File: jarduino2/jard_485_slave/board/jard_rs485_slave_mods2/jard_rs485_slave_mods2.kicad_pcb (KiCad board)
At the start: 2 copper layers, 79.2 x 30 mm, 43 parts, among them J1 POWER, J3 Débit, J4 Niveaux, J6 EV1, Q4 BPC_FMMT38C, Q6 P03P4L-04, U1 BPC_Mod485, U6 BPC_DHT22

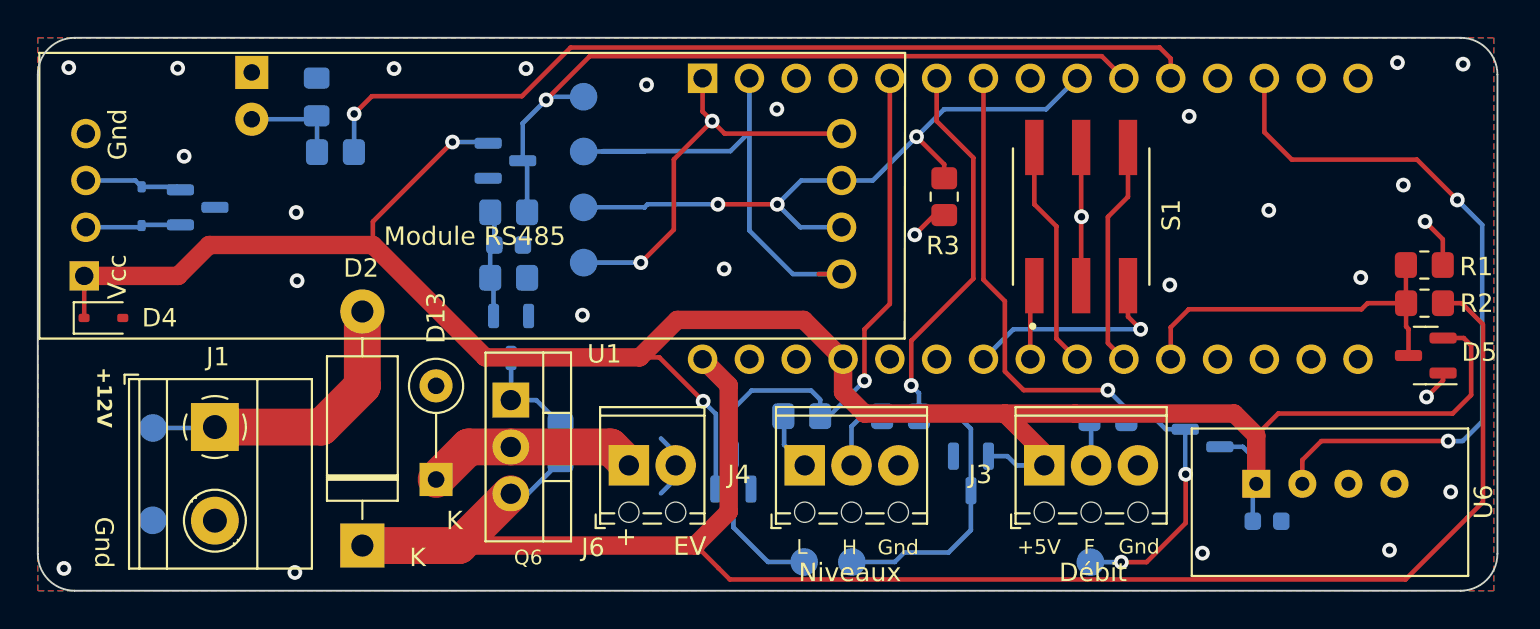
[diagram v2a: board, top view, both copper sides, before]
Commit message: Agrandissement pastilles Mod RS485
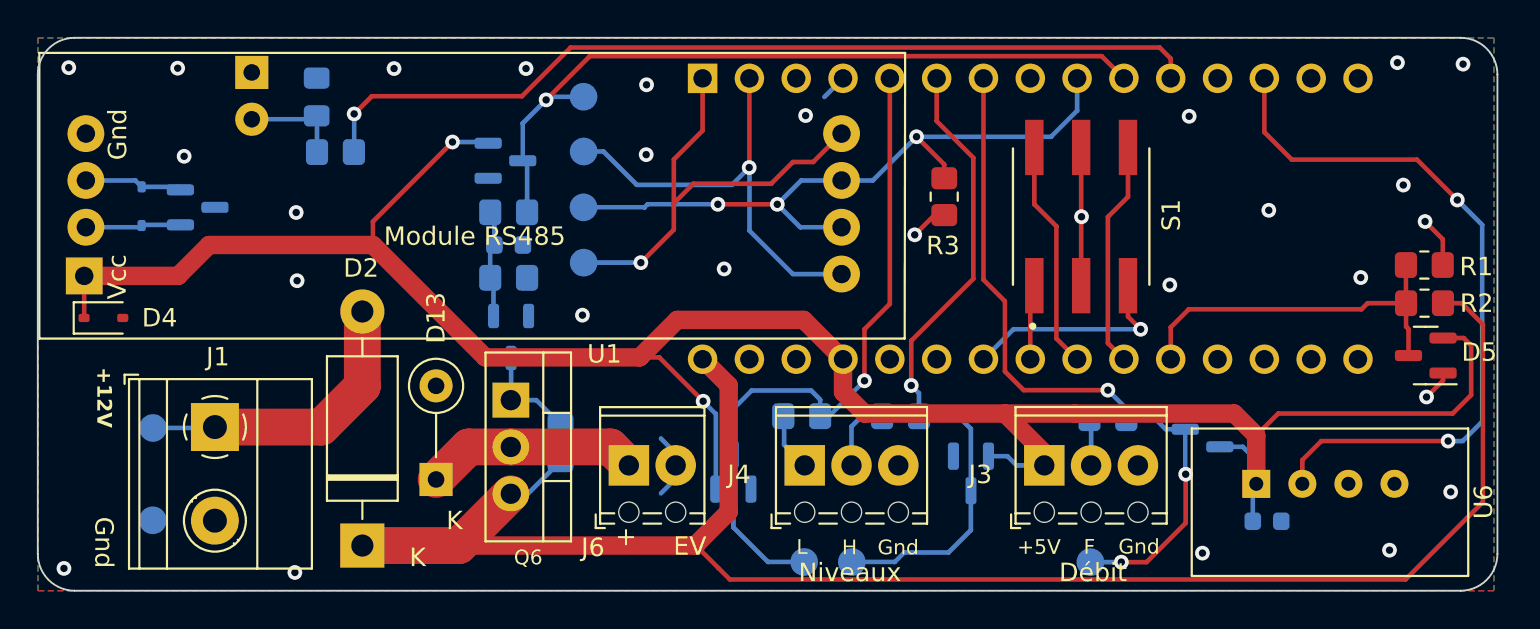
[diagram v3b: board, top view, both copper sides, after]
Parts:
- U1: value BPC_Mod485 -> Arduino_Mod_RS485
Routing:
- net TX: track 22.2 -> 25.2 mm, vias 2 -> 1
- net RX: track 27.2 -> 24.4 mm, vias 0 -> 1
- net GND: track 17.6 -> 19.1 mm, vias 27 -> 28
- net TX_EN: track 36.8 -> 37.8 mm
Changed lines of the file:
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@@
   (title_block
     (title "Carte de commande d'un OYA - Esclave RS485")
-    (date "2024-05-04")
+    (date "2024-05-17")
     (rev "F0")
     (company "BPC")
@@
         (effects (font (size 1 1) (thickness 0.15)))
     )
+    (fp_text user "${REFERENCE}" (at 6.92 0 90) (layer "F.Fab")
+        (effects (font (size 1 1) (thickness 0.15)))
+    )
     (fp_text user "K" (at 0 -2.2 90) (layer "F.Fab")
-        (effects (font (size 1 1) (thickness 0.15)))
-    )
-    (fp_text user "${REFERENCE}" (at 6.92 0 90) (layer "F.Fab")
         (effects (font (size 1 1) (thickness 0.15)))
     )
@@
         (effects (font (size 1 1) (thickness 0.15)))
     )
-    (fp_text value "BPC_Mod485" (at 8.89 19.05) (layer "F.Fab") hide
+    (fp_text value "Arduino_Mod_RS485" (at 8.89 19.05) (layer "F.Fab") hide
         (effects (font (size 1 1) (thickness 0.15)))
     )
@@
     (fp_line (start 12 -2.54) (end 12 44.46)
       (stroke (width 0.12) (type solid)) (layer "F.Fab"))
-    (pad "1" thru_hole rect (at -0.1 -0.09 90) (size 1.6 1.6) (drill 1) (layers "*.Cu" "*.Mask")
+    (pad "1" thru_hole rect (at -0.1 -0.09 90) (size 2 2) (drill 1) (layers "*.Cu" "*.Mask")
       (net 1 "+5V") (pinfunction "Vcc") (pintype "power_in"))
-    (pad "2" thru_hole oval (at 2.54 0 90) (size 1.6 1.6) (drill 1) (layers "*.Cu" "*.Mask")
+    (pad "2" thru_hole oval (at 2.54 0 90) (size 2 2) (drill 1) (layers "*.Cu" "*.Mask")
       (net 17 "BUS_B") (pinfunction "B") (pintype "tri_state"))
-    (pad "3" thru_hole oval (at 5.08 0 90) (size 1.6 1.6) (drill 1) (layers "*.Cu" "*.Mask")
+    (pad "3" thru_hole oval (at 5.08 0 90) (size 2 2) (drill 1) (layers "*.Cu" "*.Mask")
       (net 16 "BUS_A") (pinfunction "A") (pintype "tri_state"))
-    (pad "4" thru_hole oval (at 7.62 0 90) (size 1.6 1.6) (drill 1) (layers "*.Cu" "*.Mask")
+    (pad "4" thru_hole oval (at 7.62 0 90) (size 2 2) (drill 1) (layers "*.Cu" "*.Mask")
       (net 2 "GND") (pinfunction "Gnd") (pintype "power_in"))
-    (pad "5" thru_hole oval (at 7.62 41 90) (size 1.6 1.6) (drill 1) (layers "*.Cu" "*.Mask")
+    (pad "5" thru_hole oval (at 7.62 41 90) (size 2 2) (drill 1) (layers "*.Cu" "*.Mask")
       (net 9 "TX") (pinfunction "DI") (pintype "input"))
-    (pad "6" thru_hole oval (at 5.08 41 90) (size 1.6 1.6) (drill 1) (layers "*.Cu" "*.Mask")
+    (pad "6" thru_hole oval (at 5.08 41 90) (size 2 2) (drill 1) (layers "*.Cu" "*.Mask")
       (net 8 "TX_EN") (pinfunction "DE") (pintype "input"))
-    (pad "7" thru_hole oval (at 2.54 41 90) (size 1.6 1.6) (drill 1) (layers "*.Cu" "*.Mask")
+    (pad "7" thru_hole oval (at 2.54 41 90) (size 2 2) (drill 1) (layers "*.Cu" "*.Mask")
       (net 8 "TX_EN") (pinfunction "RE") (pintype "input"))
-    (pad "8" thru_hole oval (at 0 41 90) (size 1.6 1.6) (drill 1) (layers "*.Cu" "*.Mask")
+    (pad "8" thru_hole oval (at 0 41 90) (size 2 2) (drill 1) (layers "*.Cu" "*.Mask")
       (net 5 "RX") (pinfunction "RO") (pintype "output"))
     (model "${BPCLIBS}/bpc/3d/rs485.stp"
@@
         (effects (font (size 1 1) (thickness 0.15)))
     )
+    (fp_text user "K" (at 1.6 0.9 90) (layer "F.Fab")
+        (effects (font (size 1 1) (thickness 0.15)))
+    )
     (fp_text user "${REFERENCE}" (at 2.54 -2.47 90) (layer "F.Fab")
-        (effects (font (size 1 1) (thickness 0.15)))
-    )
-    (fp_text user "K" (at 1.6 0.9 90) (layer "F.Fab")
         (effects (font (size 1 1) (thickness 0.15)))
     )
@@
   (via (at 188.66 96.77) (size 0.8) (drill 0.4) (layers "F.Cu" "B.Cu") (net 2))
   (via (at 127.34 115.81) (size 0.8) (drill 0.4) (layers "F.Cu" "B.Cu") (free) (net 2))
+  (via (at 146.4 93.14) (size 0.8) (drill 0.4) (layers "F.Cu" "B.Cu") (free) (net 2))
   (via (at 186.73 114.6) (size 0.8) (drill 0.4) (layers "F.Cu" "B.Cu") (free) (net 2))
   (via (at 115.07 88.42) (size 0.8) (drill 0.4) (layers "F.Cu" "B.Cu") (free) (net 2))
@@
   (via (at 142.94 101.85) (size 0.8) (drill 0.4) (layers "F.Cu" "B.Cu") (free) (net 2))
   (via (at 176.58 114.76) (size 0.8) (drill 0.4) (layers "F.Cu" "B.Cu") (free) (net 2))
-  (via (at 153.49 90.67) (size 0.8) (drill 0.4) (layers "F.Cu" "B.Cu") (free) (net 2))
+  (via (at 155.05 91.02) (size 0.8) (drill 0.4) (layers "F.Cu" "B.Cu") (free) (net 2))
   (via (at 175.86 91.06) (size 0.8) (drill 0.4) (layers "F.Cu" "B.Cu") (free) (net 2))
   (via (at 190.05 111.44) (size 0.8) (drill 0.4) (layers "F.Cu" "B.Cu") (free) (net 2))
   (segment (start 148 110) (end 148 109.34) (width 0.25) (layer "B.Cu") (net 2))
+  (segment (start 157.08 89) (end 156.07 90.01) (width 0.25) (layer "B.Cu") (net 2))
   (segment (start 148 110.72) (end 147.2 111.52) (width 0.25) (layer "B.Cu") (net 2))
   (segment (start 148 110) (end 148 110.72) (width 0.25) (layer "B.Cu") (net 2))
@@
   (segment (start 137.938 99.822) (end 137.938 98.269) (width 0.25) (layer "B.Cu") (net 4))
   (segment (start 137.938 98.269) (end 138.163 98.044) (width 0.25) (layer "B.Cu") (net 4))
-  (segment (start 157 99.62) (end 155.754 99.62) (width 0.25) (layer "F.Cu") (net 5))
-  (segment (start 152 91.92) (end 152 89) (width 0.25) (layer "B.Cu") (net 5))
+  (segment (start 152 93.83) (end 152 89) (width 0.25) (layer "F.Cu") (net 5))
+  (segment (start 151.99 93.84) (end 152 93.83) (width 0.25) (layer "F.Cu") (net 5))
+  (via (at 151.99 93.84) (size 0.8) (drill 0.4) (layers "F.Cu" "B.Cu") (net 5))
+  (segment (start 152 93.85) (end 151.99 93.84) (width 0.25) (layer "B.Cu") (net 5))
+  (segment (start 151.05 94.78) (end 151.99 93.84) (width 0.25) (layer "B.Cu") (net 5))
   (segment (start 157 99.62) (end 154.36 99.62) (width 0.25) (layer "B.Cu") (net 5))
-  (segment (start 152 91.92) (end 150.97 92.95) (width 0.25) (layer "B.Cu") (net 5))
-  (segment (start 144.04 92.97) (end 146.32 92.97) (width 0.25) (layer "B.Cu") (net 5))
-  (segment (start 144.06 92.95) (end 144.04 92.97) (width 0.25) (layer "B.Cu") (net 5))
+  (segment (start 143.01 92.97) (end 144.08 92.97) (width 0.25) (layer "B.Cu") (net 5))
   (segment (start 154.36 99.62) (end 152 97.26) (width 0.25) (layer "B.Cu") (net 5))
-  (segment (start 152 97.26) (end 152 91.92) (width 0.25) (layer "B.Cu") (net 5))
-  (segment (start 143.01 92.97) (end 144.04 92.97) (width 0.25) (layer "B.Cu") (net 5))
-  (segment (start 150.97 92.95) (end 144.06 92.95) (width 0.25) (layer "B.Cu") (net 5))
+  (segment (start 144.08 92.97) (end 145.89 94.78) (width 0.25) (layer "B.Cu") (net 5))
+  (segment (start 145.89 94.78) (end 151.05 94.78) (width 0.25) (layer "B.Cu") (net 5))
+  (segment (start 152 97.26) (end 152 93.85) (width 0.25) (layer "B.Cu") (net 5))
   (segment (start 190.65 101.2) (end 191.8 102.35) (width 0.25) (layer "F.Cu") (net 6))
   (segment (start 149.098 114.35) (end 150.318 115.57) (width 0.25) (layer "F.Cu") (net 6))
@@
   (segment (start 158.698 94.54) (end 157 94.54) (width 0.25) (layer "B.Cu") (net 8))
   (segment (start 153.34 96.01) (end 153.515 95.835) (width 0.25) (layer "B.Cu") (net 8))
+  (segment (start 168.371 92.169) (end 161.069 92.169) (width 0.25) (layer "B.Cu") (net 8))
   (segment (start 161.069 92.169) (end 158.698 94.54) (width 0.25) (layer "B.Cu") (net 8))
   (segment (start 154.81 94.54) (end 157 94.54) (width 0.25) (layer "B.Cu") (net 8))
+  (segment (start 169.78 89) (end 169.78 90.76) (width 0.25) (layer "B.Cu") (net 8))
   (segment (start 143 96) (end 146.31 96) (width 0.25) (layer "B.Cu") (net 8))
   (segment (start 150.29 95.835) (end 146.475 95.835) (width 0.25) (layer "B.Cu") (net 8))
@@
   (segment (start 154.76 97.08) (end 157 97.08) (width 0.25) (layer "B.Cu") (net 8))
   (segment (start 146.31 96) (end 146.32 96.01) (width 0.25) (layer "B.Cu") (net 8))
-  (segment (start 168.102 90.678) (end 162.56 90.678) (width 0.25) (layer "B.Cu") (net 8))
-  (segment (start 169.78 89) (end 168.102 90.678) (width 0.25) (layer "B.Cu") (net 8))
   (segment (start 146.475 95.835) (end 146.31 96) (width 0.25) (layer "B.Cu") (net 8))
-  (segment (start 162.56 90.678) (end 161.069 92.169) (width 0.25) (layer "B.Cu") (net 8))
+  (segment (start 169.78 90.76) (end 168.371 92.169) (width 0.25) (layer "B.Cu") (net 8))
   (segment (start 153.515 95.835) (end 154.81 94.54) (width 0.25) (layer "B.Cu") (net 8))
-  (segment (start 149.98 91.32) (end 147.9 93.4) (width 0.25) (layer "F.Cu") (net 9))
-  (segment (start 149.46 90.8) (end 149.46 89) (width 0.25) (layer "F.Cu") (net 9))
+  (segment (start 154.36 93.54) (end 153.18 94.72) (width 0.25) (layer "F.Cu") (net 9))
+  (segment (start 148.96 94.72) (end 147.9 95.78) (width 0.25) (layer "F.Cu") (net 9))
+  (segment (start 149.46 89) (end 149.46 91.84) (width 0.25) (layer "F.Cu") (net 9))
   (segment (start 147.9 97.21) (end 146.11 99) (width 0.25) (layer "F.Cu") (net 9))
-  (segment (start 157 92) (end 150.66 92) (width 0.25) (layer "F.Cu") (net 9))
-  (segment (start 150.66 92) (end 149.98 91.32) (width 0.25) (layer "F.Cu") (net 9))
-  (segment (start 147.9 93.4) (end 147.9 97.21) (width 0.25) (layer "F.Cu") (net 9))
-  (segment (start 149.98 91.32) (end 149.46 90.8) (width 0.25) (layer "F.Cu") (net 9))
+  (segment (start 157 92) (end 155.46 93.54) (width 0.25) (layer "F.Cu") (net 9))
+  (segment (start 155.46 93.54) (end 154.36 93.54) (width 0.25) (layer "F.Cu") (net 9))
+  (segment (start 149.46 91.84) (end 147.9 93.4) (width 0.25) (layer "F.Cu") (net 9))
+  (segment (start 147.9 95.78) (end 147.9 97.21) (width 0.25) (layer "F.Cu") (net 9))
+  (segment (start 153.18 94.72) (end 148.96 94.72) (width 0.25) (layer "F.Cu") (net 9))
+  (segment (start 147.9 93.4) (end 147.9 95.78) (width 0.25) (layer "F.Cu") (net 9))
   (via (at 146.11 99) (size 0.8) (drill 0.4) (layers "F.Cu" "B.Cu") (net 9))
-  (via (at 149.98 91.32) (size 0.8) (drill 0.4) (layers "F.Cu" "B.Cu") (net 9))
   (segment (start 143.01 99) (end 146.11 99) (width 0.25) (layer "B.Cu") (net 9))
   (segment (start 185.21 101.53) (end 175.838 101.53) (width 0.25) (layer "F.Cu") (net 10))
